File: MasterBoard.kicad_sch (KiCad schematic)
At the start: 9 parts, among them U8 CD4066BPW

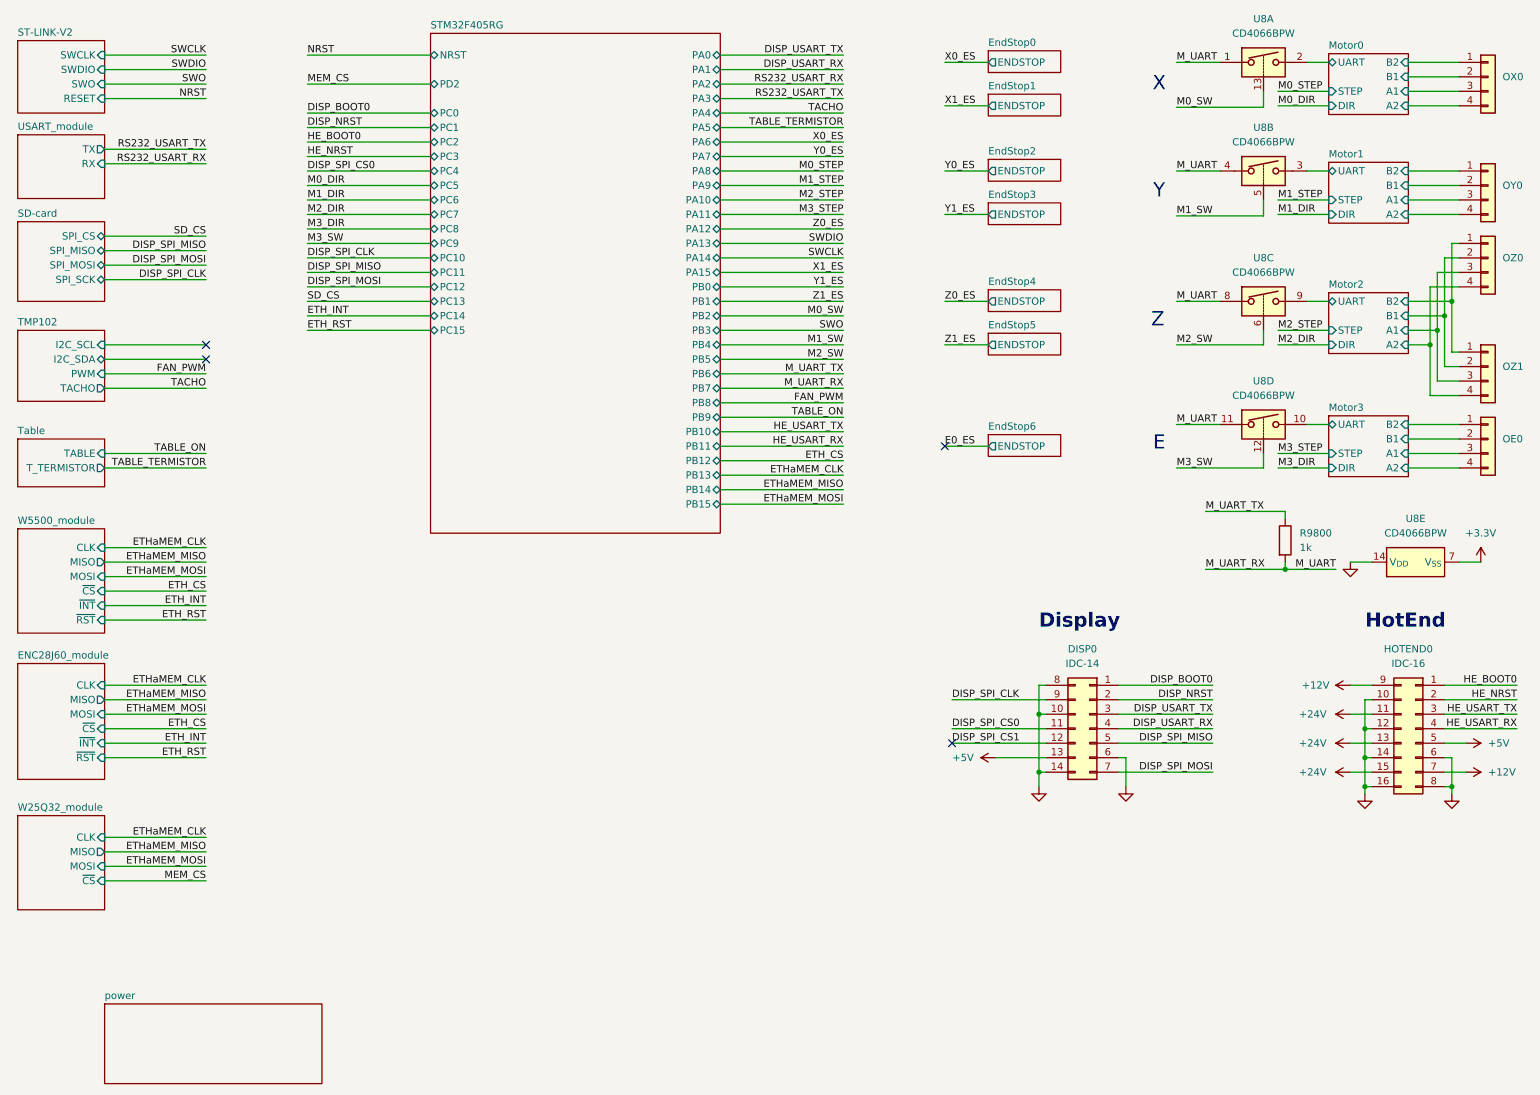
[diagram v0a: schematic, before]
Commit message: Обновил плату, убрал много элементов. посчитал, что так будет лучше
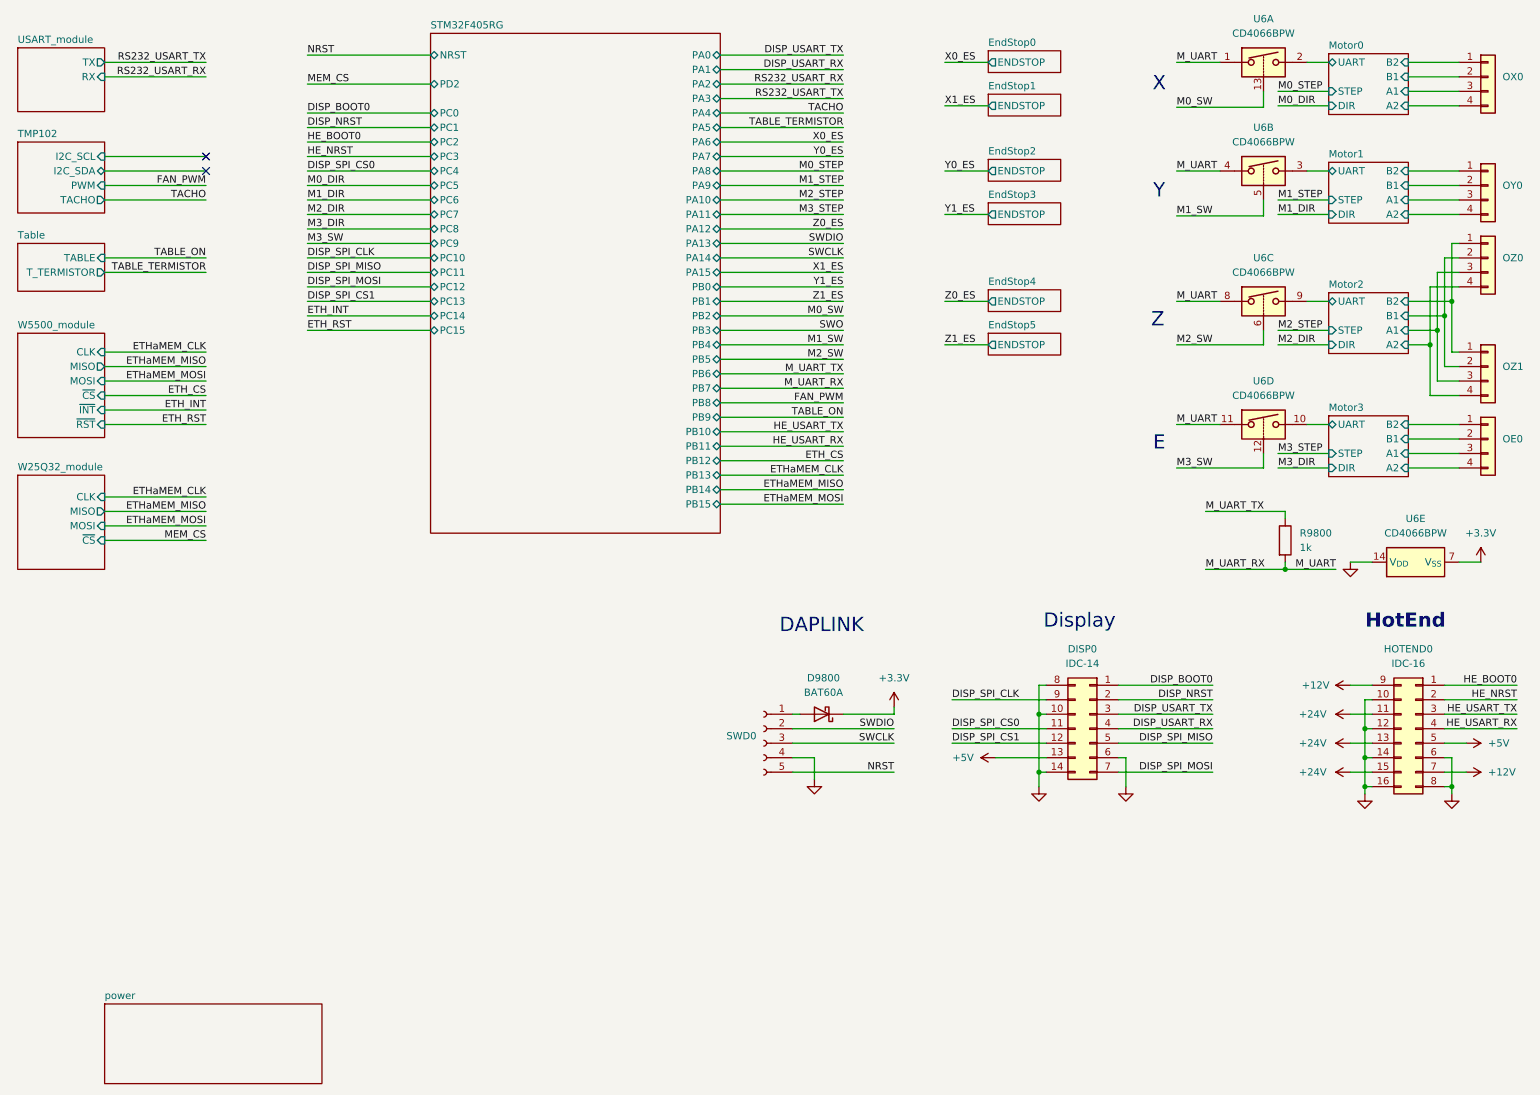
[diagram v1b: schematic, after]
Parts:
- added D9800: BAT60A, Diode_SMD:D_SOD-323, symbol Diode:BAT60A
- added SWD0: Conn_01x05_Socket, Connector_PinSocket_2.54mm:PinSocket_1x05_P2.54mm_Vertical, symbol Connector:Conn_01x05_Socket
- renumbered U8 to U6
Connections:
- net +3.3V: now also D9800.1 (K)
- net GND: now also SWD0.4 (Pin_4)
- net NRST: now also SWD0.5 (Pin_5)
- net SWCLK: now also SWD0.3 (Pin_3)
- net SWDIO: now also SWD0.2 (Pin_2)
- new net: D9800.2 (A), SWD0.1 (Pin_1)
- no-connect marks 4 -> 2
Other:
- removed sheet ENC28J60_module
- removed sheet EndStop6
- removed sheet SD-card
- removed sheet ST-LINK-V2
- note added: "DAPLINK"

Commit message: Обновил/почистил схему
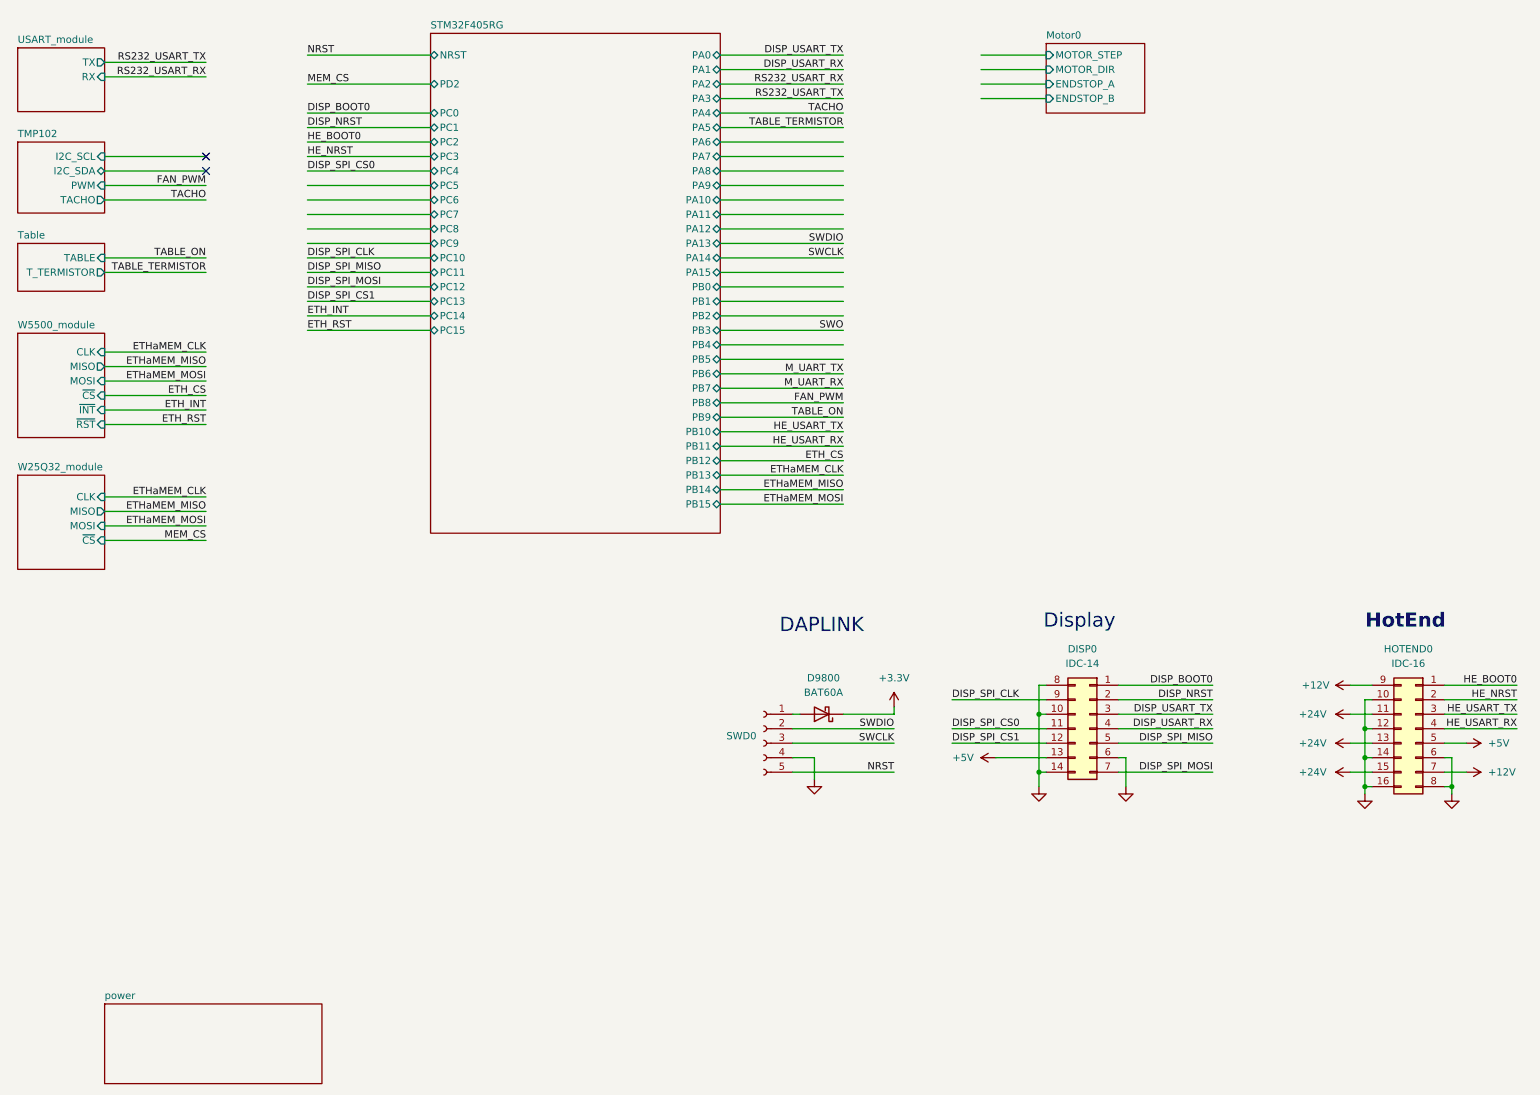
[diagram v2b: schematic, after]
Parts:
- removed OE0: M3, Connector_JST:JST_XH_B4B-XH-A_1x04_P2.50mm_Vertical, symbol Connector_Generic:Conn_01x04
- removed OX0: M0, Connector_JST:JST_XH_B4B-XH-A_1x04_P2.50mm_Vertical, symbol Connector_Generic:Conn_01x04
- removed OY0: M1, Connector_JST:JST_XH_B4B-XH-A_1x04_P2.50mm_Vertical, symbol Connector_Generic:Conn_01x04
- removed OZ0, OZ1: M2, Connector_JST:JST_XH_B4B-XH-A_1x04_P2.50mm_Vertical, symbol Connector_Generic:Conn_01x04
- removed R9800: 1k, Resistor_SMD:R_0805_2012Metric, symbol Device:R
- removed U6: CD4066BPW, Package_SO:TSSOP-14_4.4x5mm_P0.65mm, symbol Analog_Switch:CD4066BPW
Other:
- removed sheet EndStop0
- removed sheet EndStop1
- removed sheet EndStop2
- removed sheet EndStop3
- removed sheet EndStop4
- removed sheet EndStop5
- removed sheet Motor1
- removed sheet Motor2
- removed sheet Motor3
- sheet Motor0 ports: added ENDSTOP_A, ENDSTOP_B, MOTOR_DIR, MOTOR_STEP; removed A1, A2, B1, B2, DIR, STEP, UART
- note removed: "E"
- note removed: "X"
- note removed: "Y"
- note removed: "Z"

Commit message: Множественная перекомпоновка
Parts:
- removed DISP0: IDC-14, Connector_IDC:IDC-Header_2x07_P2.54mm_Vertical, symbol Connector_Generic:Conn_02x07_Top_Bottom
- removed HOTEND0: IDC-16, Connector_IDC:IDC-Header_2x08_P2.54mm_Vertical, symbol Connector_Generic:Conn_02x08_Top_Bottom
- added RP1: Raspberry_Pi_2_3, Connector_PinHeader_2.54mm:PinHeader_2x20_P2.54mm_Vertical, symbol Connector:Raspberry_Pi_2_3
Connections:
- net +3.3V: now also RP1.1 (3V3), RP1.17 (3V3)
- net +5V: now also RP1.2 (5V), RP1.4 (5V)
- net GND: now also RP1.14 (GND), RP1.20 (GND), RP1.25 (GND), RP1.30 (GND), RP1.34 (GND), RP1.39 (GND), RP1.6 (GND), RP1.9 (GND)
- no-connect marks 2 -> 0
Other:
- removed sheet STM32F405RG
- removed sheet TMP102
- removed sheet Table
- removed sheet W25Q32_module
- removed sheet W5500_module
- added sheet Motor1 (schematics/Motor.kicad_sch)
- added sheet Motor2 (schematics/Motor.kicad_sch)
- added sheet Motor3 (schematics/Motor.kicad_sch)
- added sheet Motor4 (schematics/Motor.kicad_sch)
- added sheet Motor5 (schematics/Motor.kicad_sch)
- added sheet Motor6 (schematics/Motor.kicad_sch)
- added sheet Motor7 (schematics/Motor.kicad_sch)
- added sheet Motor8 (schematics/Motor.kicad_sch)
- added sheet Motor9 (schematics/Motor.kicad_sch)
- added sheet STM32F407VG (schematics/STM32F407VG.kicad_sch)
- added sheet periphery (schematics/periphery.kicad_sch)
- note removed: "Display"
- note removed: "HotEnd"
- moved on the sheet: D9800, SWD0

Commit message: Вывел все выводы, но еще не соединил
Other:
- sheet STM32F407VG ports: added BOOT0, NRST, PA0, PA1, PA10, PA11, PA12, PA13, PA14, PA15, PA2, PA3, PA4, PA5, PA6, PA7, PA8, PA9, PB0, PB1, PB10, PB11, PB12, PB13, PB14, PB15, PB2, PB3, PB4, PB5, PB6, PB7, PB8, PB9, PC0, PC1, PC10, PC11, PC12, PC13, PC14, PC15, PC2, PC3, PC4, PC5, PC6, PC7, PC8, PC9, PD0, PD1, PD10, PD11, PD12, PD13, PD14, PD15, PD2, PD3, PD4, PD5, PD6, PD7, PD8, PD9, PE0, PE1, PE10, PE11, PE12, PE13, PE14, PE15, PE2, PE3, PE4, PE5, PE6, PE7, PE8, PE9; removed none
